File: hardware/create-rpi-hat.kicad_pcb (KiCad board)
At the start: 2 copper layers, 65 x 30 mm, 22 parts, among them IC1 LMZ21701SILT, J1 Roomba_conn, J2 USB_B_Micro, J3 RaspberryPi GPIO connector, U2 TXS0102DCT, U3 FT230XS, U4 NUP2202

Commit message: Removed power pours and made more space for the buck module
The latter is against module's layout recommendations, but makes
soldering/rework easier
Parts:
- TP1: renamed from TP1 (PG)
- moved C3 4.50 mm to (107.5, 58.9)
- moved C2 3.43 mm to (103.3, 63.0)
- moved R2 3.34 mm to (111.2, 62.5)
- moved R1 3.34 mm to (111.2, 64.4)
- moved R3 3.34 mm to (111.2, 60.5)
- moved IC1 3.25 mm to (107.5, 63.1)
- moved TP1 3.25 mm to (116.4, 61.0)
- moved C1 1.91 mm to (108.4, 67.0)
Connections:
- J3 pad 14: Net-(J3-Pad14) -> GND
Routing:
- net +5V: track 45.4 -> 65.5 mm, vias 4 -> 1
- net /VIN_Roomba: track 4.61 -> 19.8 mm, vias 1 -> 2
- net /USBVBUS: track 10.2 -> 23.2 mm
- net +3V3: track 17.5 -> 27.5 mm
- net GND: track 26.8 -> 17.1 mm, vias 0 -> 103
- net /RX_TTL: track 42.8 -> 37.3 mm
- net /3.3V_FTDI: track 20.0 -> 15.1 mm, vias 1 -> 0
- net /TX_TTL: track 32.1 -> 34.0 mm
- net Net-(C1-Pad1): track 1.33 -> 2.67 mm
- net Net-(IC1-Pad2): track 2.55 -> 3.16 mm
- net /PG: track 9.50 -> 9.08 mm, vias 0 -> 2
- added copper zone on B.Cu, net GND
- removed copper zone on B.Cu, net +3V3
- removed copper zone on B.Cu, net +5V
- removed copper zone on B.Cu, net /3.3V_FTDI
- removed copper zone on B.Cu, net /3.3V_RPi
- removed copper zone on B.Cu, net /USBVBUS
- removed copper zone on B.Cu, net /VIN_Roomba
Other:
- net class Power: clearance 0.3 -> 0.2; via_dia 1.6 -> 1; via_drill 0.8 -> 0.5

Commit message: Add a bit of vanity
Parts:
- added G***: LOGO, kicad-libs:OYTIS, B.Cu at (85.8, 69.3)

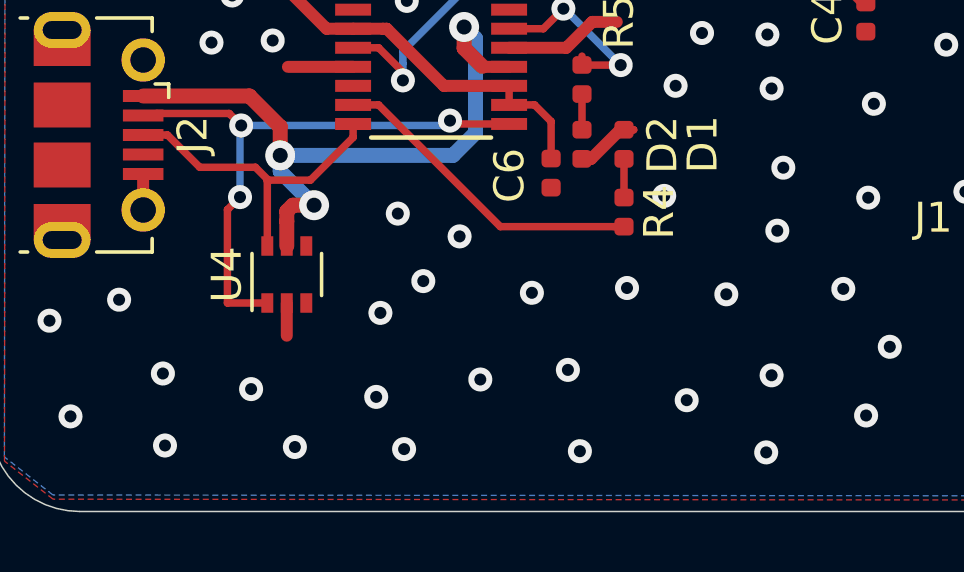
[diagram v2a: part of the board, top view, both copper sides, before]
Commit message: First revision (ordered on Aisler) and postmortem
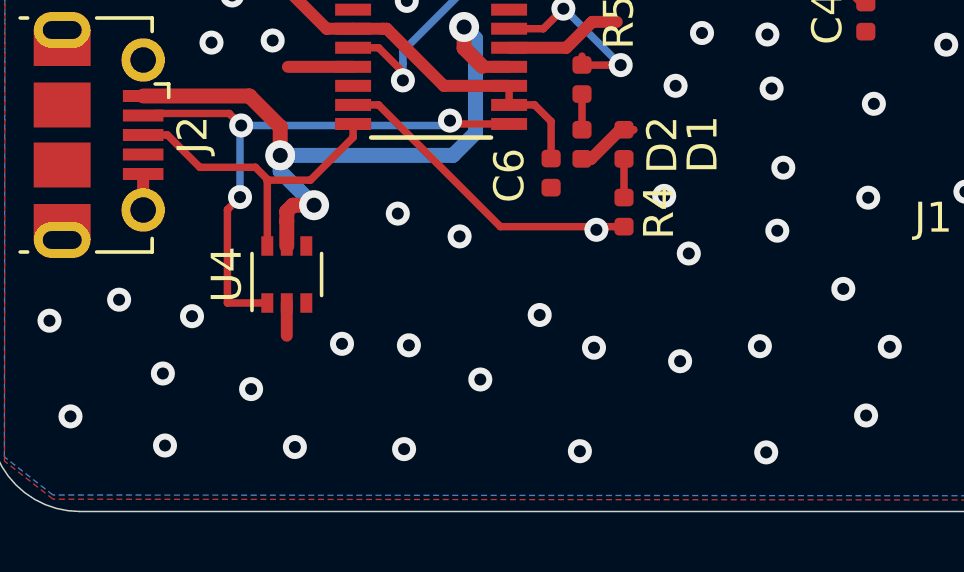
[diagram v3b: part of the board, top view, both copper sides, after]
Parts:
- moved G*** 8.42 mm to (79.1, 74.4)
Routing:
- net Net-(R4-Pad2): vias 0 -> 1
- net GND: vias 103 -> 102

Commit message: Revision 0.9 (also ordered on Aisler)
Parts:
- removed the G*** at (79.1, 74.4)
- added C7: 100n, Capacitor_SMD:C_0402_1005Metric, F.Cu at (79.2, 65.7)
- added C8: 4.7u, Capacitor_SMD:C_0402_1005Metric, F.Cu at (80.6, 65.7)
- added G***: LOGO, kicad-libs:Create2Pi, B.Cu at (106.1, 61.4)
- added REF**: MountingHole_2.7mm_M2.5_Pad, MountingHole:MountingHole_2.7mm_M2.5_Pad, F.Cu at (63.5, 53.5)
- added REF**: MountingHole_2.7mm_M2.5_Pad, MountingHole:MountingHole_2.7mm_M2.5_Pad, F.Cu at (63.5, 76.5)
- added REF**: MountingHole_2.7mm_M2.5_Pad, MountingHole:MountingHole_2.7mm_M2.5_Pad, F.Cu at (121.5, 53.5)
- added REF**: MountingHole_2.7mm_M2.5_Pad, MountingHole:MountingHole_2.7mm_M2.5_Pad, F.Cu at (121.5, 76.5)
- J1: value Roomba_conn -> Mini-DIN-8; footprint kicad-libs:CUI_TB001-500-05BE -> kicad-libs:CUI_MD-80SM
- moved C5 7.90 mm to (89.2, 62.7), turned to 90 degrees
- moved C4 7.48 mm to (96.4, 61.4)
- moved J1 5.82 mm to (99.2, 70.8), turned to 180 degrees
- moved D2 2.74 mm to (82.5, 67.8)
- moved R5 2.74 mm to (82.5, 65.6)
- moved D1 2.74 mm to (83.9, 67.8)
- moved R4 2.74 mm to (83.9, 70.0)
- turned U2 to 180 degrees
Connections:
- C4 pad 1: +5V -> +3V3
- C5 pad 2: +3V3 -> +5V
- J1 pad 2: /TX_Roomba -> /VIN_Roomba
- J1 pad 5: GND -> /TX_Roomba
- U2 pad 1: /TX_TTL -> /TX_Roomba
- U2 pad 3: +5V -> +3V3
- U2 pad 4: /TX_Roomba -> /TX_TTL
- U2 pad 5: /RX_Roomba -> /RX_TTL
- U2 pad 6: +5V -> +3V3
- U2 pad 7: +3V3 -> +5V
- U2 pad 8: /RX_TTL -> /RX_Roomba
- U3 pad 1: /RX_TTL -> /TX_TTL
- U3 pad 4: /TX_TTL -> /RX_TTL
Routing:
- net +5V: track 65.5 -> 71.5 mm
- net /TX_Roomba: track 17.4 -> 11.9 mm, vias 0 -> 2
- net /USBVBUS: track 23.2 -> 26.5 mm
- net /RX_TTL: track 37.3 -> 40.1 mm, vias 1 -> 3
- net Net-(R4-Pad2): track 10.7 -> 13.5 mm, vias 1 -> 0
- net +3V3: track 27.5 -> 29.5 mm
- net /VIN_Roomba: track 19.8 -> 18.0 mm, vias 2 -> 0
- net GND: track 17.1 -> 16.1 mm, vias 102 -> 83
- net /PG: track 9.08 -> 10.1 mm
- net Net-(R5-Pad2): track 6.36 -> 5.67 mm, vias 2 -> 0
- net /RX_Roomba: track 17.4 -> 17.9 mm, vias 0 -> 2
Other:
- board text removed: "GND [6,7]"
- board text removed: "NC [5]"
- board text removed: "RX [3]"
- board text removed: "TX [4]"
- board text removed: "VIN [1,2]"
